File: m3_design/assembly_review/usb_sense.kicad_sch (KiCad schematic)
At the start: 3 parts

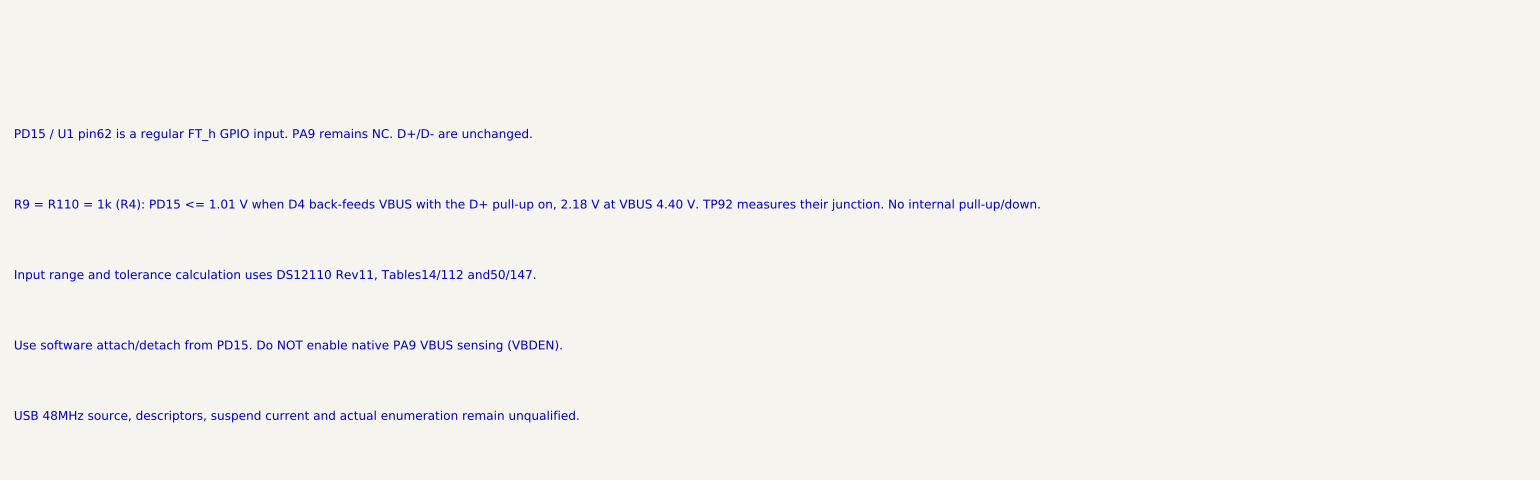
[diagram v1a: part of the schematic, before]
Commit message: M3-ASSY-R8: re-placed layout with planned-bus routing, owner-accepted deviations
R8 keeps R7's circuit, RF strip and CH1 pyro block (copied rigidly and
hash-asserted) and re-places everything else: U1 rotated so its free
pins face the RF strip, each block beside the U1 face it talks to, input
protection back at J1, and a fresh deterministic build (r8_build.sh)
with planned-bus routing, no autorouter and no patch stages.

Against R7: signal track 3.36 m -> 1.50 m, signal vias 217 -> 55,
simplicity index 100 -> 15.3, gate exceptions 74 -> 3, hard routing-rule
instances 10 -> 1, 7.7 A neck rise 38/30/44 -> 17.6/14.8/22.3 C,
unreferenced critical samples 27.9 % -> 11.1 %, non-pyro nets within
3 mm of armed copper 23 -> 7.

- Gate: check_r8 (pin contract from pin_table.tsv, F10 separation,
  battery/pyro clearance, loader-pin rule, rigid hashes), route_check
  profile r8, scorecard, dc_solve --necks, reference_audit, paste_check
- Review: passes 2, 3 and 4 found 0 Critical / 0 Major in all eight
  dimensions; pass 5 re-checked the final board (routing, planes,
  integrity) with 0 Critical / 0 Major
- Owner accepted the R8 deviation list on 2026-10-20, including the C10
  vibration item and the listed agent decisions

Board SHA-256 cc044ea0922ff826df19af9d9726d92c096ab2b127025b55d123d8772e5fb4a7.
tools/check.sh: DRC 0, unconnected 0, parity 0, ERC 0; audit, silk,
R8 contract, routing hygiene (0 failing, 3 allowlisted), actuator
contract and fit OK. Before ordering: consign U4, JLC tab acceptance,
cost/stock run within 24 h.

Co-Authored-By: Claude Opus 5.5 <noreply@anthropic.com>
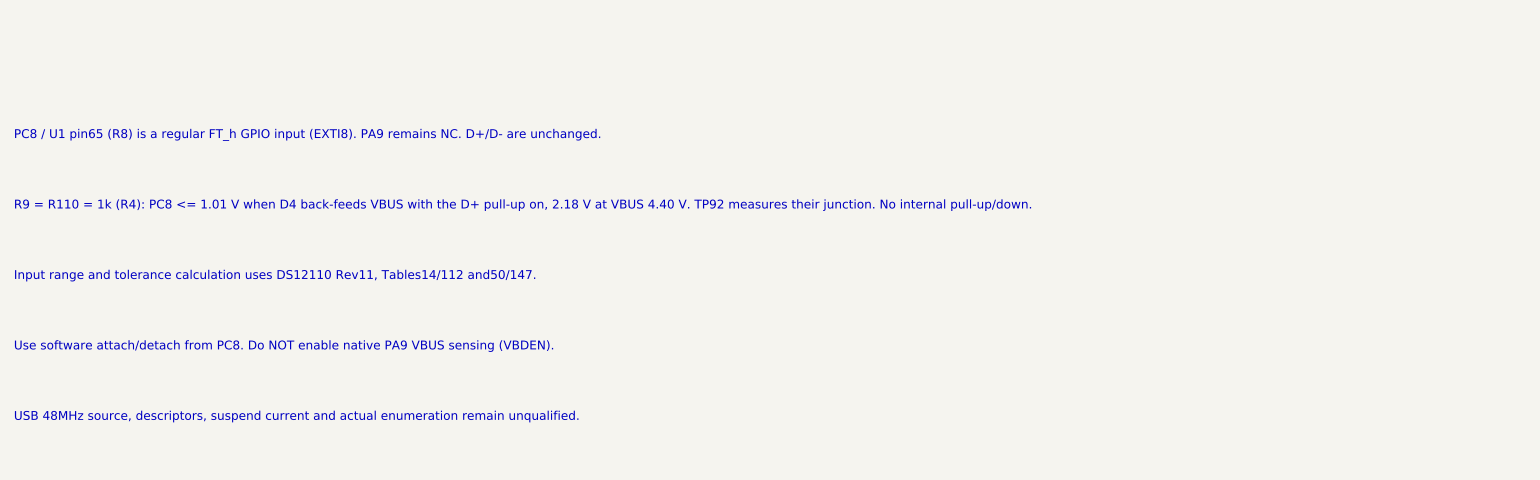
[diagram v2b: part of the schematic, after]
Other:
- note added: "PC8 / U1 pin65 (R8) is a regular FT_h GPIO input (EXTI8). PA9 remains NC. D+/D- are unchanged."
- note added: "R9 = R110 = 1k (R4): PC8 <= 1.01 V when D4 back-feeds VBUS with the D+ pull-up on, 2.18 V at VBUS 4.40 V. TP92 measures their junction. No internal pull-up/down."
- note added: "Use software attach/detach from PC8. Do NOT enable native PA9 VBUS sensing (VBDEN)."
- note removed: "PD15 / U1 pin62 is a regular FT_h GPIO input. PA9 remains NC. D+/D- are unchanged."
- note removed: "R9 = R110 = 1k (R4): PD15 <= 1.01 V when D4 back-feeds VBUS with the D+ pull-up on, 2.18 V at VBUS 4.40 V. TP92 measures their junction. No internal pull-up/down."
- note removed: "Use software attach/detach from PD15. Do NOT enable native PA9 VBUS sensing (VBDEN)."
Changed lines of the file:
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@@
 		(title "10 | USB cable presence, ordinary GPIO sensing")
 		(date "2026-09-07")
-		(rev "M3-ASSY-R7")
+		(rev "M3-ASSY-R8")
 		(company "Single-board M3 candidate; full system incomplete"))
 	(text "10 | USB cable presence, ordinary GPIO sensing"
@@
 			(justify right))
 )
-	(text "PD15 / U1 pin62 is a regular FT_h GPIO input. PA9 remains NC. D+/D- are unchanged."
+	(text "PC8 / U1 pin65 (R8) is a regular FT_h GPIO input (EXTI8). PA9 remains NC. D+/D- are unchanged."
 		(at 20.32 137.16 0)
 		(effects
@@
 			(justify left))
 )
-	(text "R9 = R110 = 1k (R4): PD15 <= 1.01 V when D4 back-feeds VBUS with the D+ pull-up on, 2.18 V at VBUS 4.40 V. TP92 measures their junction. No internal pull-up/down."
+	(text "R9 = R110 = 1k (R4): PC8 <= 1.01 V when D4 back-feeds VBUS with the D+ pull-up on, 2.18 V at VBUS 4.40 V. TP92 measures their junction. No internal pull-up/down."
 		(at 20.32 147.32 0)
 		(effects
@@
 			(justify left))
 )
-	(text "Use software attach/detach from PD15. Do NOT enable native PA9 VBUS sensing (VBDEN)."
+	(text "Use software attach/detach from PC8. Do NOT enable native PA9 VBUS sensing (VBDEN)."
 		(at 20.32 167.64 0)
 		(effects
